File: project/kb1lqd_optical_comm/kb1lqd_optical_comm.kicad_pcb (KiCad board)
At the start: 4 copper layers, 76.2 x 101.6 mm, 75 parts, among them J1 SJ1-3523N, J2 SJ-2509N, J3 SJ1-3523N, J4 Conn_01x04_Male, J5 Conn_01x02_Male, J6 SJ1-3523N, Q1 PMBF170, SW1 EG1213, SW2 EG1213, SW3 EG1213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

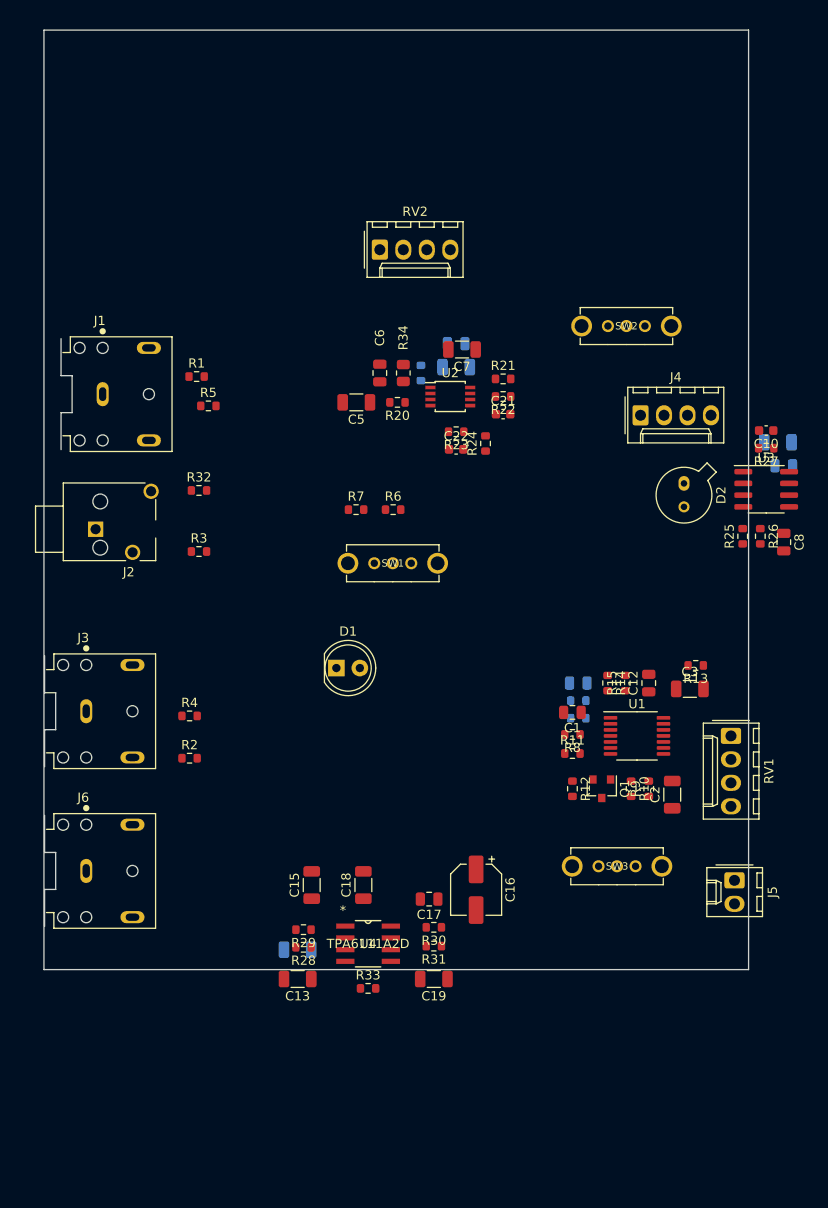
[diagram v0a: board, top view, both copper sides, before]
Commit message: Initial placement condensed.
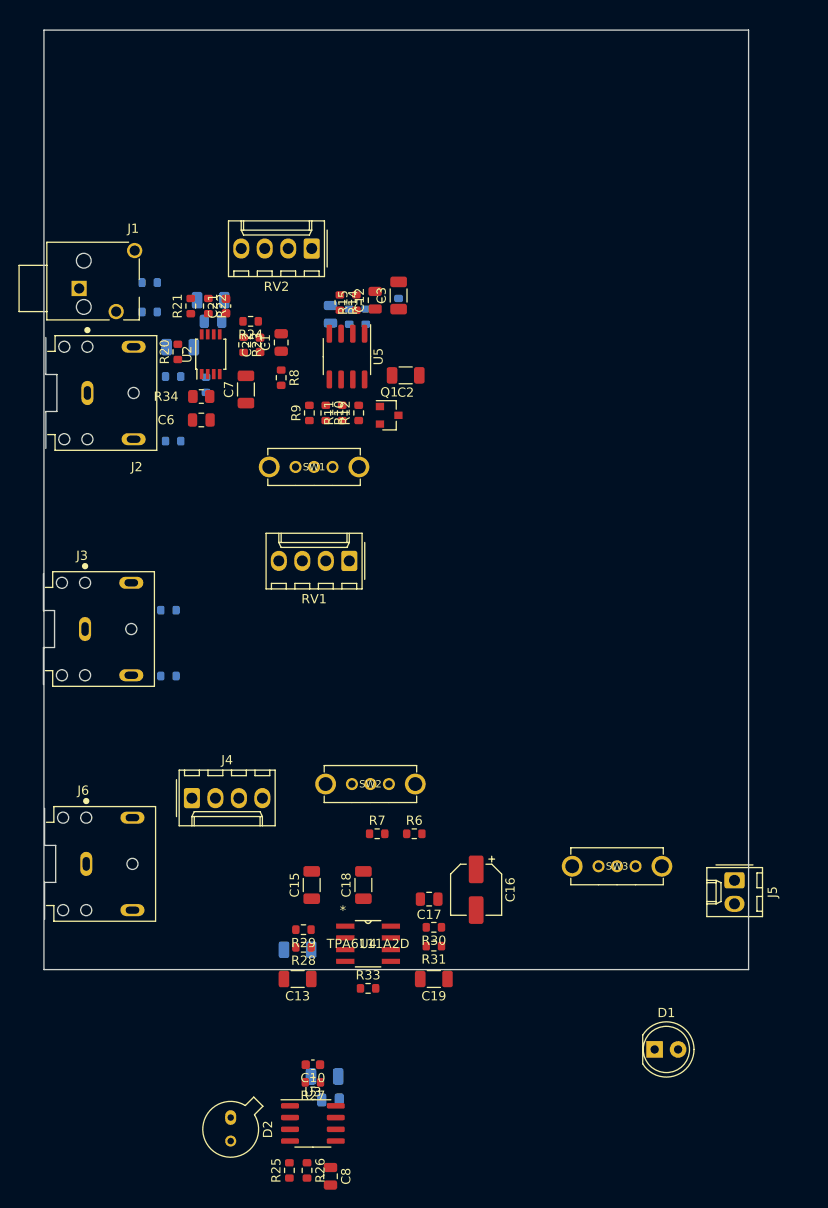
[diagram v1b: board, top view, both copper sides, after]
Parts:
- removed U1: AD8648, Package_SO:TSSOP-14_4.4x5mm_P0.65mm
- added U5: AD8646, Package_SO:SOIC-8_3.9x4.9mm_P1.27mm, F.Cu at (159.8, 60.7)
- C5, R1, R13, R2, R3, R32, R4, R5: moved to B.Cu
- moved C10 84.3 mm to (156.1, 137.3)
- moved C9 84.3 mm to (158.0, 141.1)
- moved D2 84.3 mm to (147.2, 143.0)
- moved R25 84.3 mm to (153.5, 148.7)
- moved R26 84.3 mm to (155.4, 148.7)
- moved R27 84.3 mm to (156.1, 139.2)
- moved C8 84.3 mm to (158.0, 149.4)
- moved U3 84.3 mm to (156.1, 143.6)
- moved C11 84.3 mm to (157.4, 138.6)
- moved J4 63.8 mm to (143.0, 108.5)
- moved SW2 56.7 mm to (162.3, 106.9)
- moved R9 54.8 mm to (155.7, 66.8)
- moved C2 53.7 mm to (166.1, 62.7), turned to 180 degrees
- moved D1 53.7 mm to (193.0, 135.6)
- moved C3 52.9 mm to (165.4, 54.1), turned to 90 degrees
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
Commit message: More placement. Ready for board outline update.
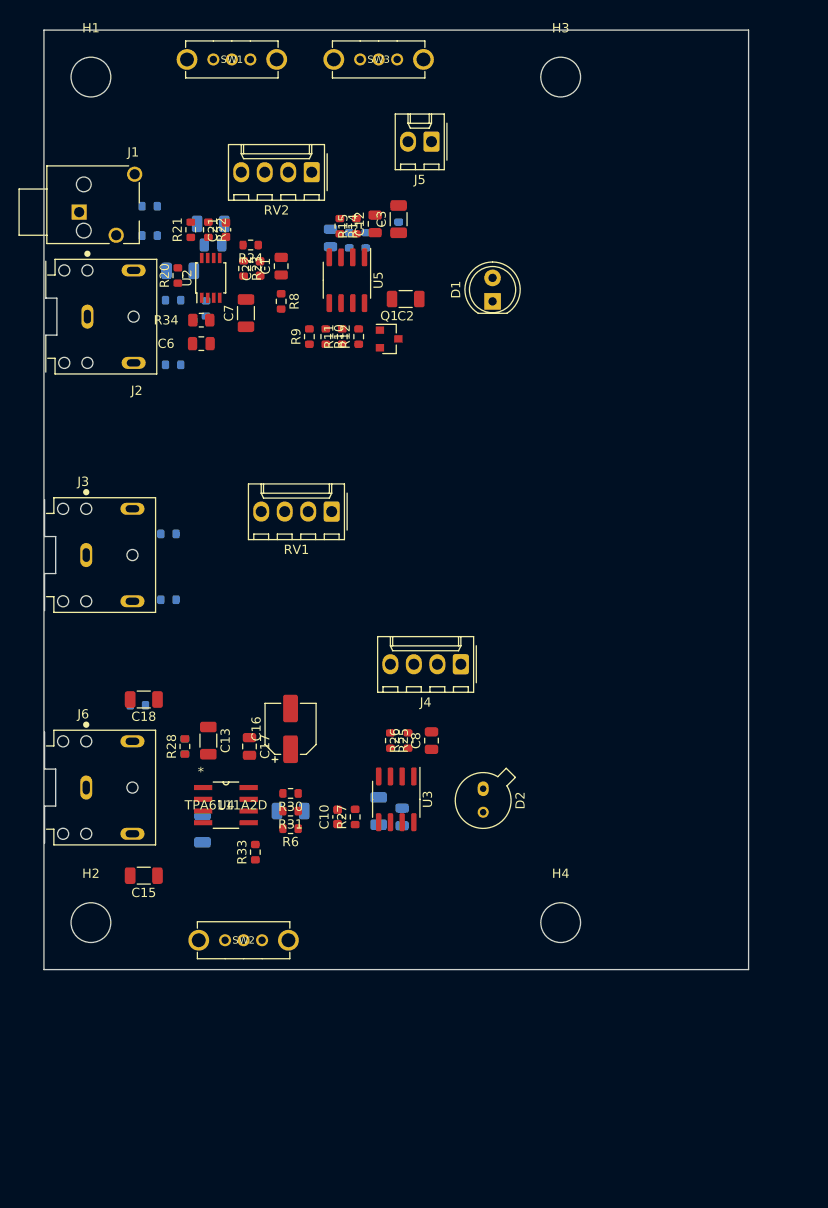
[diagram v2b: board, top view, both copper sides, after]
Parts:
- added H1: MountingHole_Pad, MountingHole:MountingHole_4.3mm_M4, F.Cu at (132.1, 30.5)
- added H2: MountingHole_Pad, MountingHole:MountingHole_4.3mm_M4, F.Cu at (132.1, 121.9)
- added H3: MountingHole_Pad, MountingHole:MountingHole_4.3mm_M4, F.Cu at (182.9, 30.5)
- added H4: MountingHole_Pad, MountingHole:MountingHole_4.3mm_M4, F.Cu at (182.9, 121.9)
- C19, R29, R7: moved to B.Cu
- moved SW3 91.0 mm to (163.2, 28.6), turned to 180 degrees
- moved J5 86.3 mm to (168.9, 37.5), turned to 180 degrees
- moved D1 82.8 mm to (175.5, 54.7), turned to 90 degrees
- moved C8 48.4 mm to (168.9, 102.2), turned to 90 degrees
- moved R25 47.7 mm to (164.5, 102.2), turned to 270 degrees
- moved R26 47.7 mm to (166.4, 102.2), turned to 90 degrees
- moved SW1 45.0 mm to (147.3, 28.6), turned to 180 degrees
- moved D2 44.8 mm to (174.5, 107.4)
- moved U3 36.2 mm to (165.1, 108.6), turned to 270 degrees
- moved J4 32.5 mm to (172.1, 94.0), turned to 180 degrees
- moved C9 31.6 mm to (165.7, 110.5), turned to 90 degrees
- moved C18 31.1 mm to (137.8, 97.8), turned to 180 degrees
- moved R7 29.4 mm to (137.2, 98.4)
- moved C11 29.3 mm to (163.2, 109.9), turned to 90 degrees
- moved R27 29.1 mm to (160.7, 110.5), turned to 90 degrees
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
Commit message: Placement done.
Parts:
- C15: moved to B.Cu
- moved J5 35.1 mm to (172.7, 72.4)
- moved RV2 31.7 mm to (158.1, 72.4)
- moved J4 11.4 mm to (172.7, 82.5)
- moved C15 10.8 mm to (142.9, 107.3)
- moved D2 8.74 mm to (181.6, 102.4)
- moved C10 8.13 mm to (165.1, 105.4)
- moved C11 8.13 mm to (169.5, 104.8)
- moved C8 8.13 mm to (175.3, 97.2)
- moved C9 8.13 mm to (172.1, 105.4)
- moved R25 8.13 mm to (170.8, 97.2)
- moved R26 8.13 mm to (172.7, 97.2)
- moved R27 8.13 mm to (167.0, 105.4)
- moved U3 8.13 mm to (171.4, 103.5)
- moved D1 6.10 mm to (181.6, 54.7)
- moved RV1 5.08 mm to (158.1, 82.5)
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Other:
- board size 76.2 x 101.6 mm -> 61 x 101.6 mm

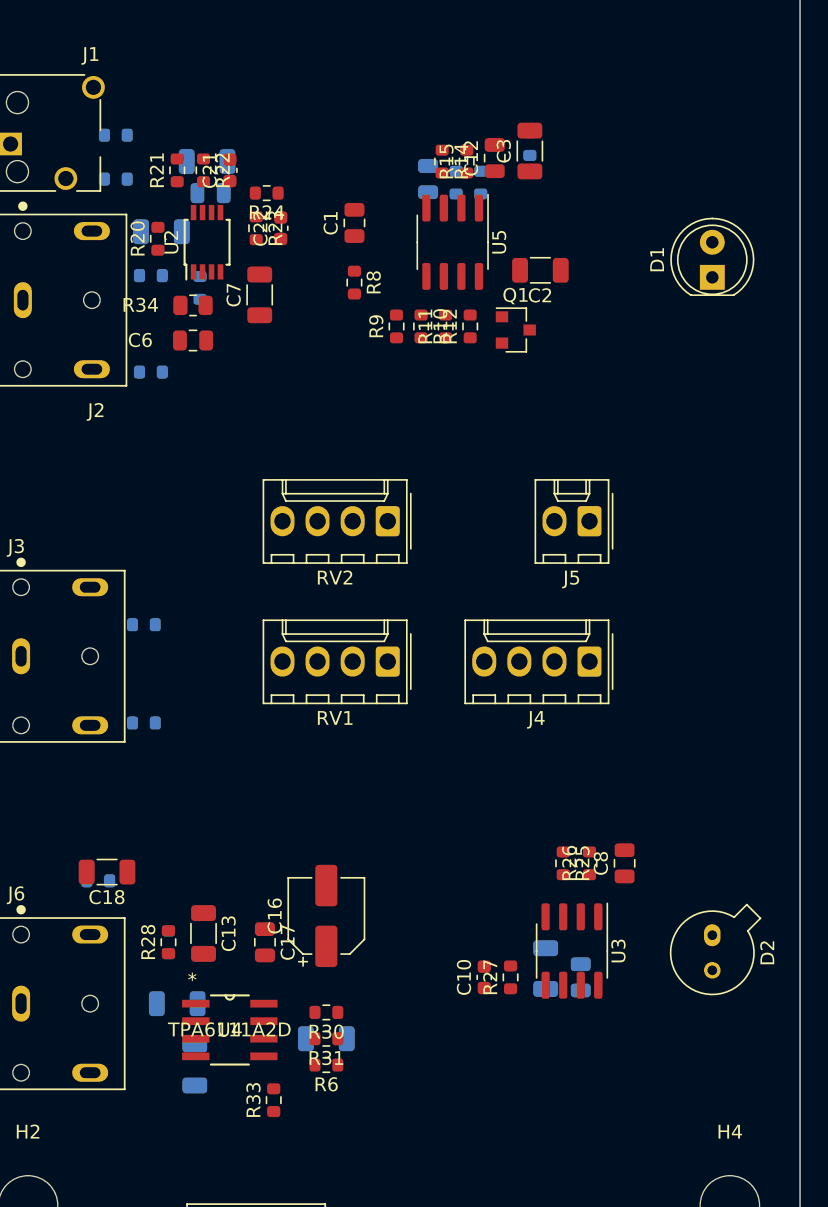
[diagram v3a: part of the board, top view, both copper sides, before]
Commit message: Moved silkscreen references.
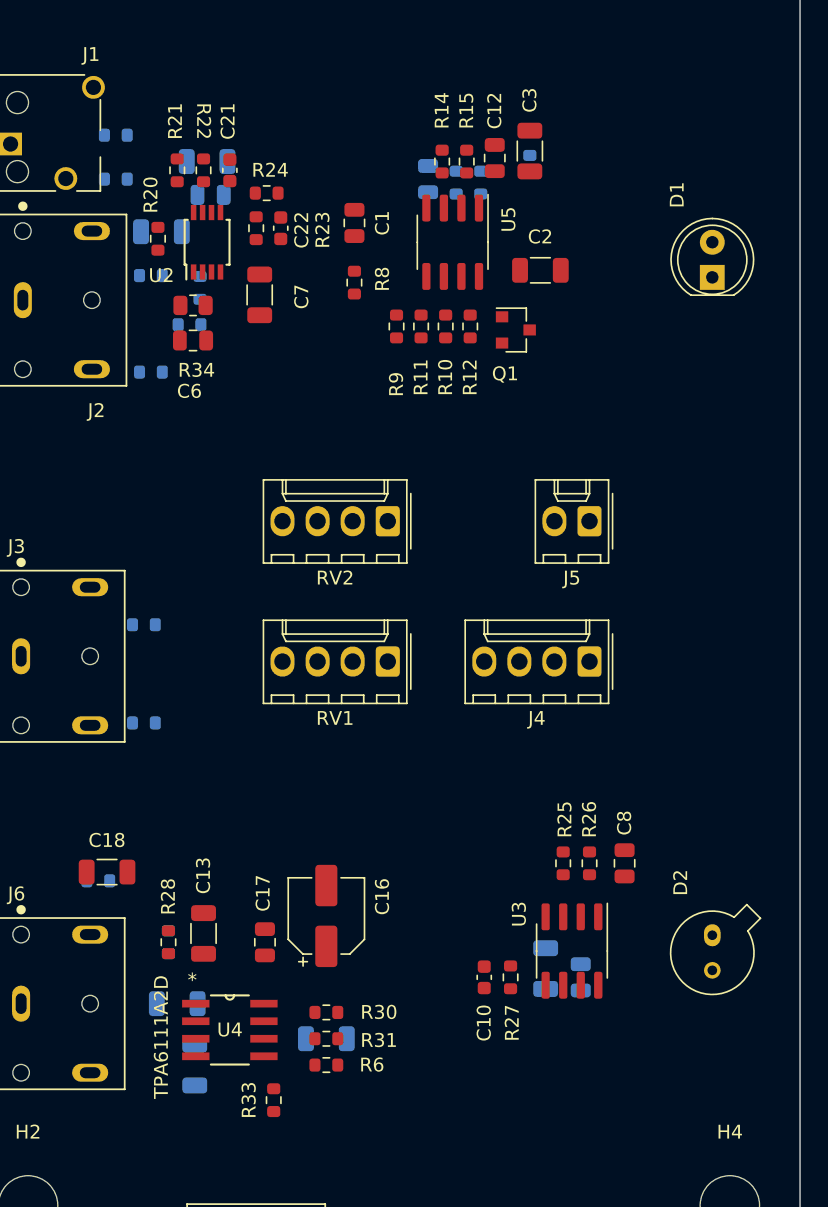
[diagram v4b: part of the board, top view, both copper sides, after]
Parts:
- moved R18 1.42 mm to (143.8, 58.2)
- moved C23 0.13 mm to (145.3, 48.8)

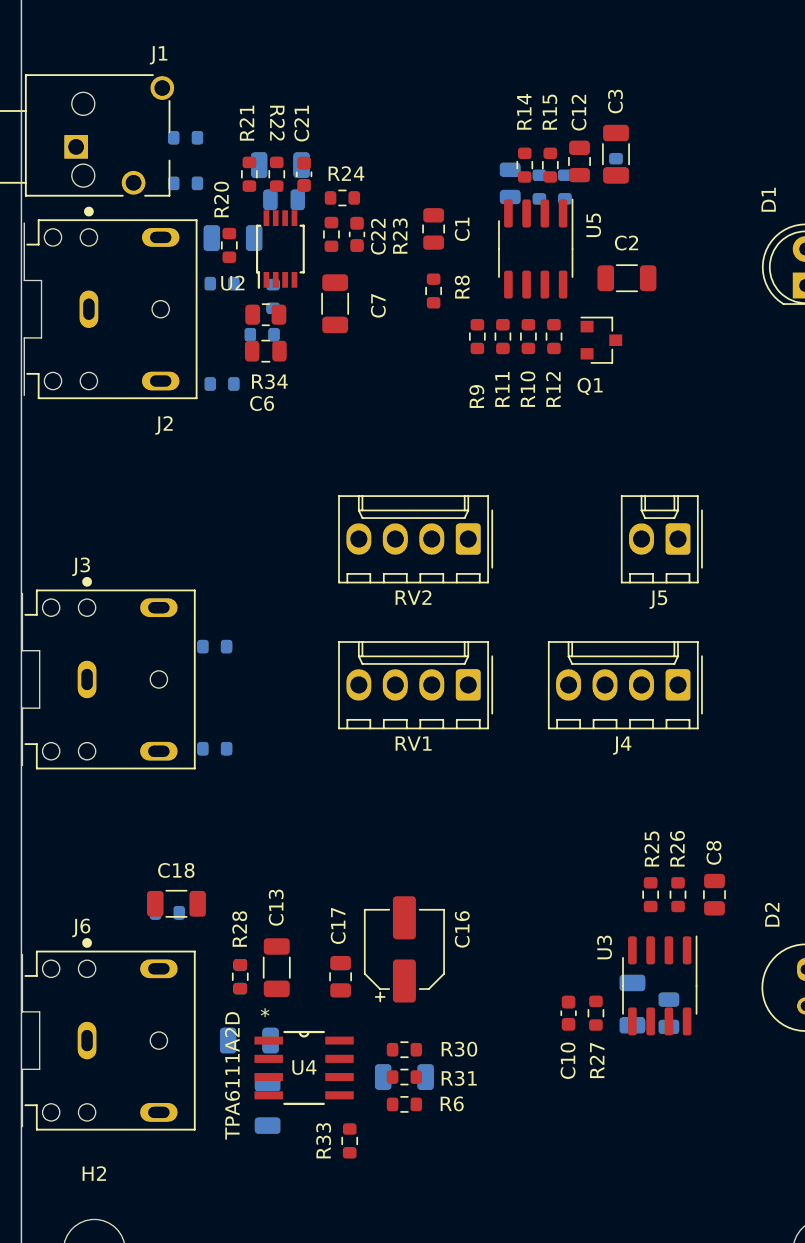
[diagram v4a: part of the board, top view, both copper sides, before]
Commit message: Most of initial routing completed.
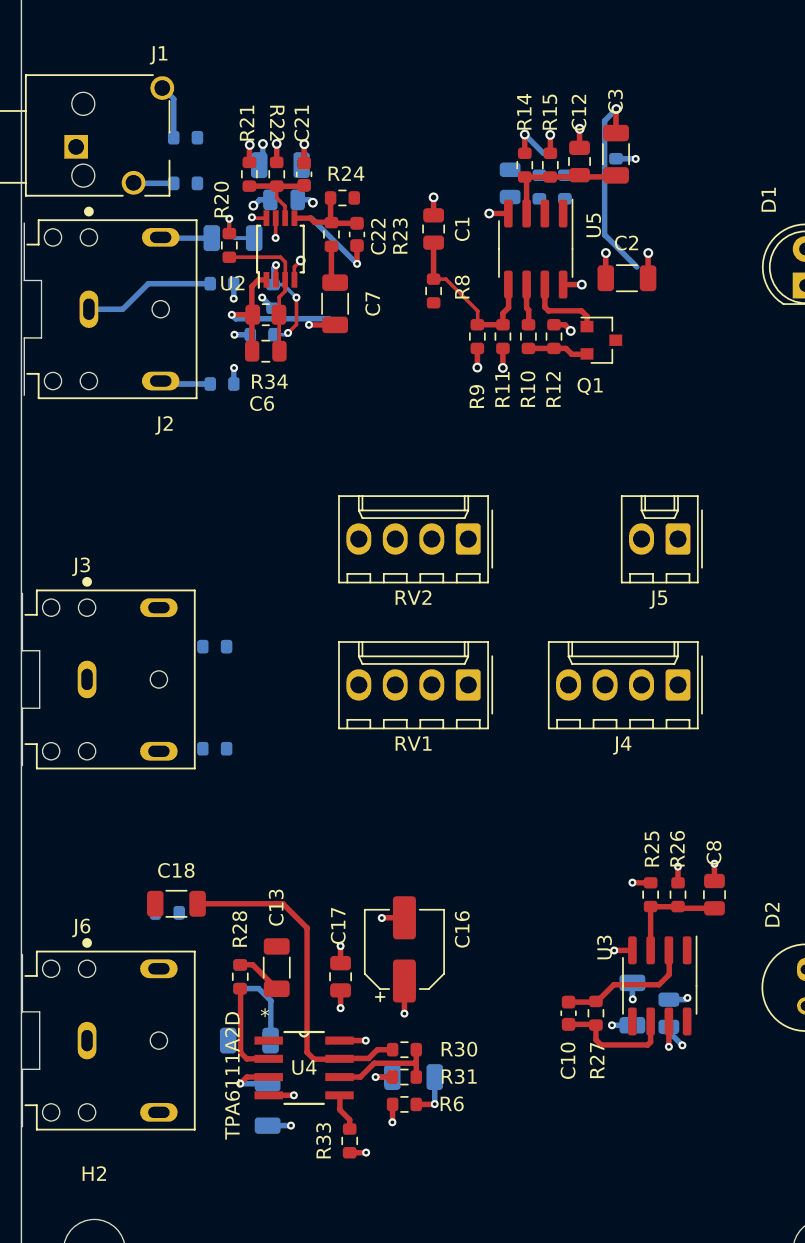
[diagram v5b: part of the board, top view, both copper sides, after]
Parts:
- moved C19 0.64 mm to (154.3, 109.9)
- turned C7 to 270 degrees
- turned R31 to 0 degrees
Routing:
- net GND: track 0.00 -> 34.9 mm, vias 0 -> 26
- net +5V: track 0.00 -> 25.2 mm, vias 0 -> 16
- net Net-(C18-Pad1): track 0.00 -> 23.5 mm
- net Net-(C6-Pad1): track 0.00 -> 15.9 mm, vias 0 -> 2
- net Net-(C3-Pad2): track 0.00 -> 13.9 mm, vias 0 -> 1
- net Net-(C1-Pad1): track 0.00 -> 12.3 mm
- net Net-(C6-Pad2): track 0.00 -> 10.5 mm
- net Net-(C10-Pad2): track 0.00 -> 9.43 mm
- net Net-(C12-Pad1): track 0.00 -> 9.20 mm
- net Net-(J1-Pad1): track 0.00 -> 9.18 mm
- net Net-(R18-Pad1): track 0.00 -> 8.45 mm, vias 0 -> 3
- net /Photodiode Transimpedance Amplifier/OUTPUT: track 0.00 -> 8.44 mm
- net Net-(R30-Pad1): track 0.00 -> 7.93 mm
- net Net-(C8-Pad1): track 0.00 -> 7.49 mm
- net /Michrophone Pre-Amp/AUDIO_OUTPUT: track 0.00 -> 7.14 mm, vias 0 -> 2
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- added copper zone on In1.Cu, net +5V
- added copper zone on In2.Cu, net GND
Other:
- net class Preferred added: clearance 0.127, trace_width 0.3048, via_dia 0.5588, via_drill 0.254
